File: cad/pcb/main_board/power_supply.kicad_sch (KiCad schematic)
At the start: 14 parts, among them U2 TLV75533PDRVR

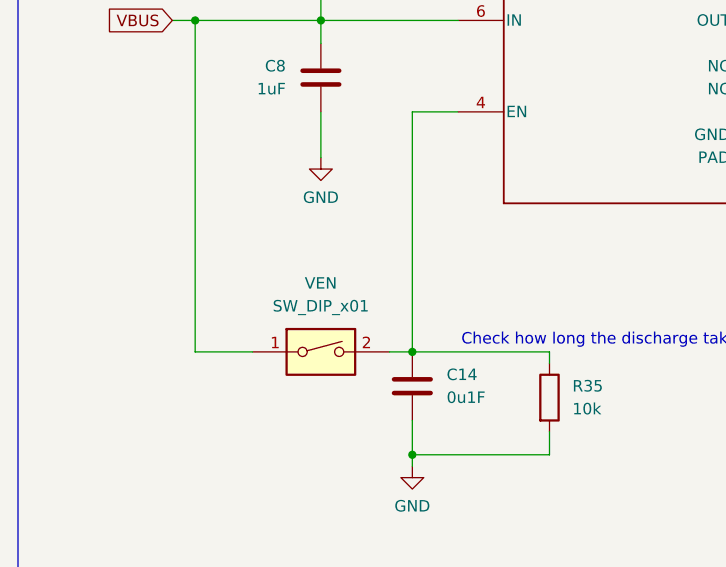
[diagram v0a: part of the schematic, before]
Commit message: Checking VBAT
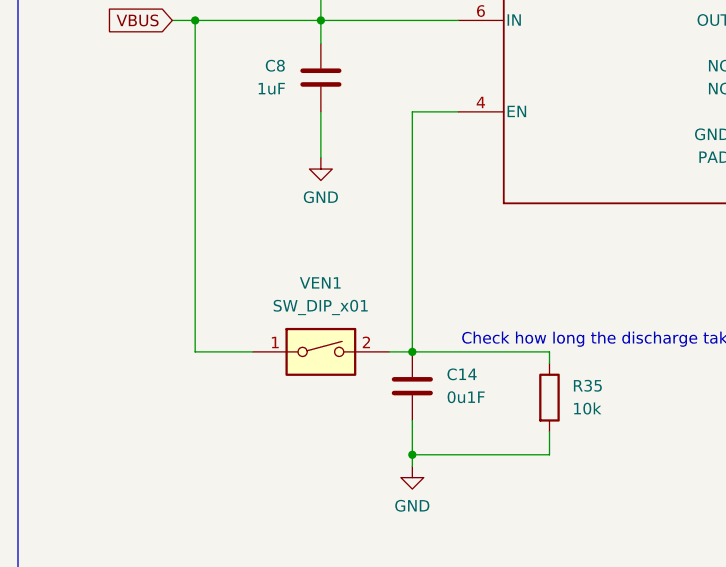
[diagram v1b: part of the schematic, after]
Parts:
- renumbered VEN to VEN1
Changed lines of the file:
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@@
 		(dnp no)
 		(fields_autoplaced yes)
-		(property "Reference" "VEN"
+		(property "Reference" "VEN1"
 			(at 80.01 151.13 0)
 			(effects
@@
 			(project "main_board"
 				(path "/6c1b8035-64fa-4797-a506-5c9583cb241c/89e1b759-e3da-4961-90e8-6f92bf79e795/8c2804c0-90ed-471e-8073-15cf7e3965b7"
-					(reference "VEN")
+					(reference "VEN1")
 					(unit 1)
 				)

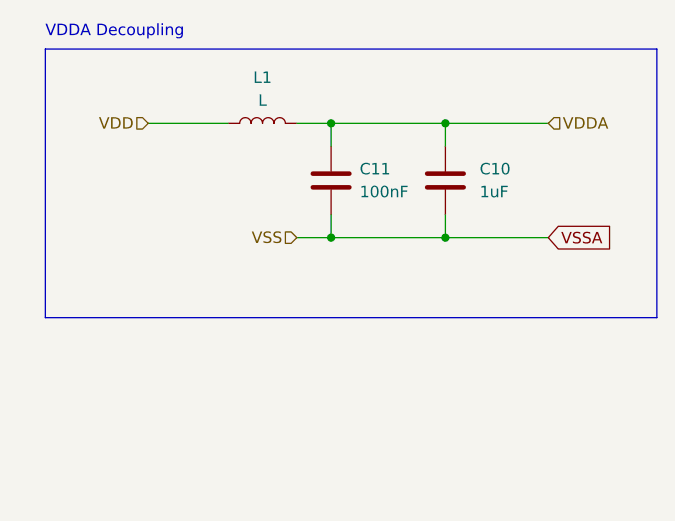
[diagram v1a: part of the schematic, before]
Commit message: DRC mostly checks out now
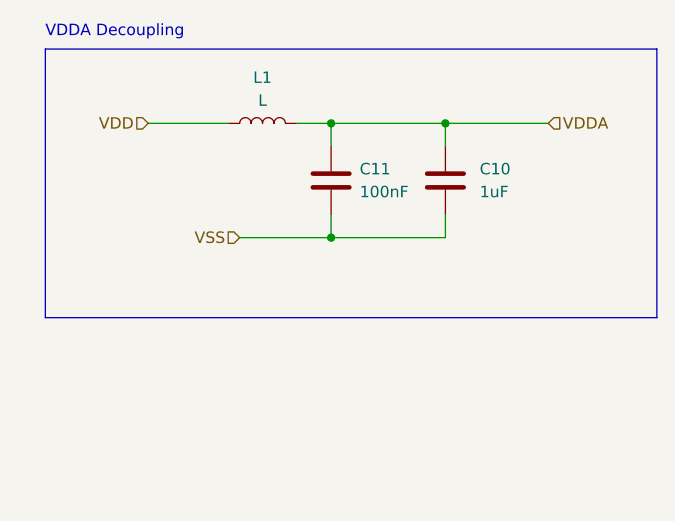
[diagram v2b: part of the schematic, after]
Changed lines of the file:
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@@
-		(color 0 0 0 0)
-	)
-	(junction
-		(at 203.2 72.39)
-		(diameter 0)
 		(color 0 0 0 0)
 	)
@@
 	(wire
 		(pts
-			(xy 214.63 72.39) (xy 203.2 72.39)
-		)
-		(stroke
-			(width 0)
-			(type default)
-		)
-	)
-	(wire
-		(pts
 			(xy 190.5 62.23) (xy 190.5 59.69)
 		)
@@
 	(wire
 		(pts
+			(xy 180.34 72.39) (xy 190.5 72.39)
+		)
+		(stroke
+			(width 0)
+			(type default)
+		)
+	)
+	(wire
+		(pts
 			(xy 102.87 72.39) (xy 102.87 69.85)
 		)
@@
 		(pts
 			(xy 170.18 59.69) (xy 179.07 59.69)
-		)
-		(stroke
-			(width 0)
-			(type default)
-		)
-	)
-	(wire
-		(pts
-			(xy 186.69 72.39) (xy 190.5 72.39)
 		)
 		(stroke
@@
 			)
 			(justify left bottom)
-		)
-	)
-	(global_label "VSSA"
-		(shape input)
-		(at 214.63 72.39 0)
-		(fields_autoplaced yes)
-		(effects
-			(font
-				(size 1.27 1.27)
-			)
-			(justify left)
-		)
-		(property "Intersheetrefs" "${INTERSHEET_REFS}"
-			(at 222.2114 72.39 0)
-			(effects
-				(font
-					(size 1.27 1.27)
-				)
-				(justify left)
-				(hide yes)
-			)
 		)
 	)
@@
 	(hierarchical_label "VSS"
 		(shape input)
-		(at 186.69 72.39 180)
+		(at 180.34 72.39 180)
 		(fields_autoplaced yes)
 		(effects

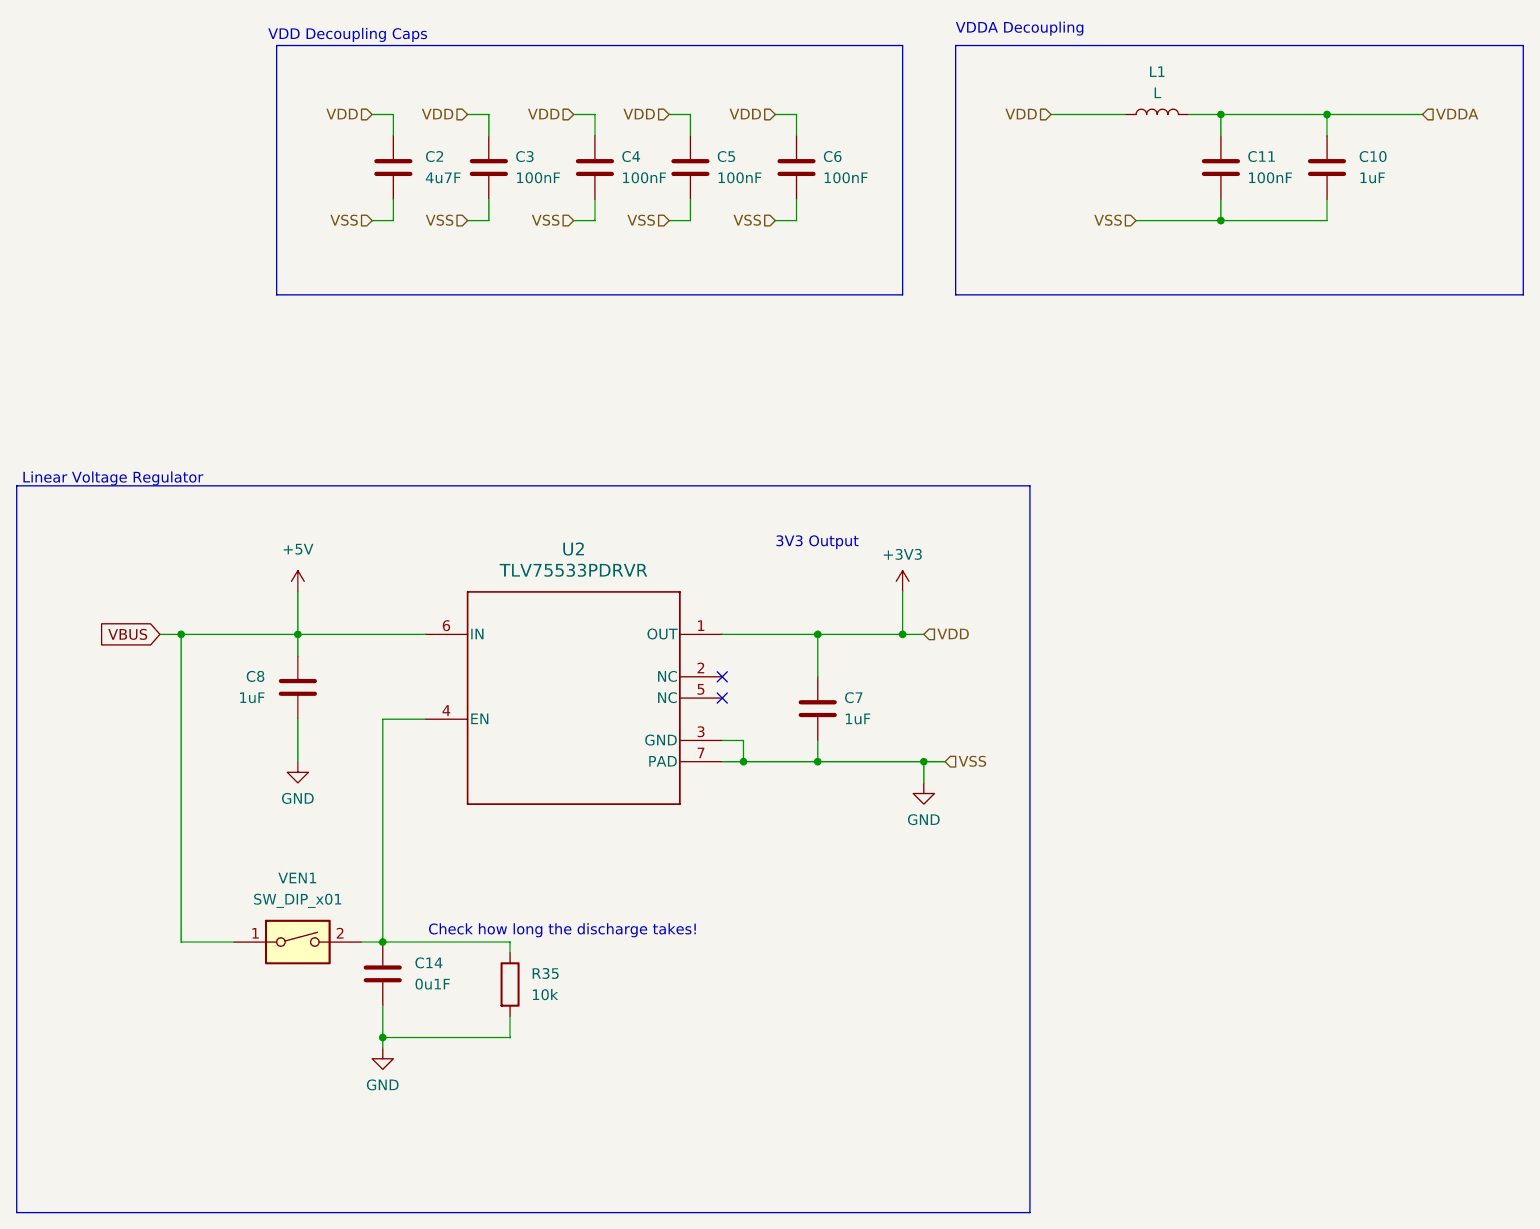
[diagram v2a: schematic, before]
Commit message: SWD connector start
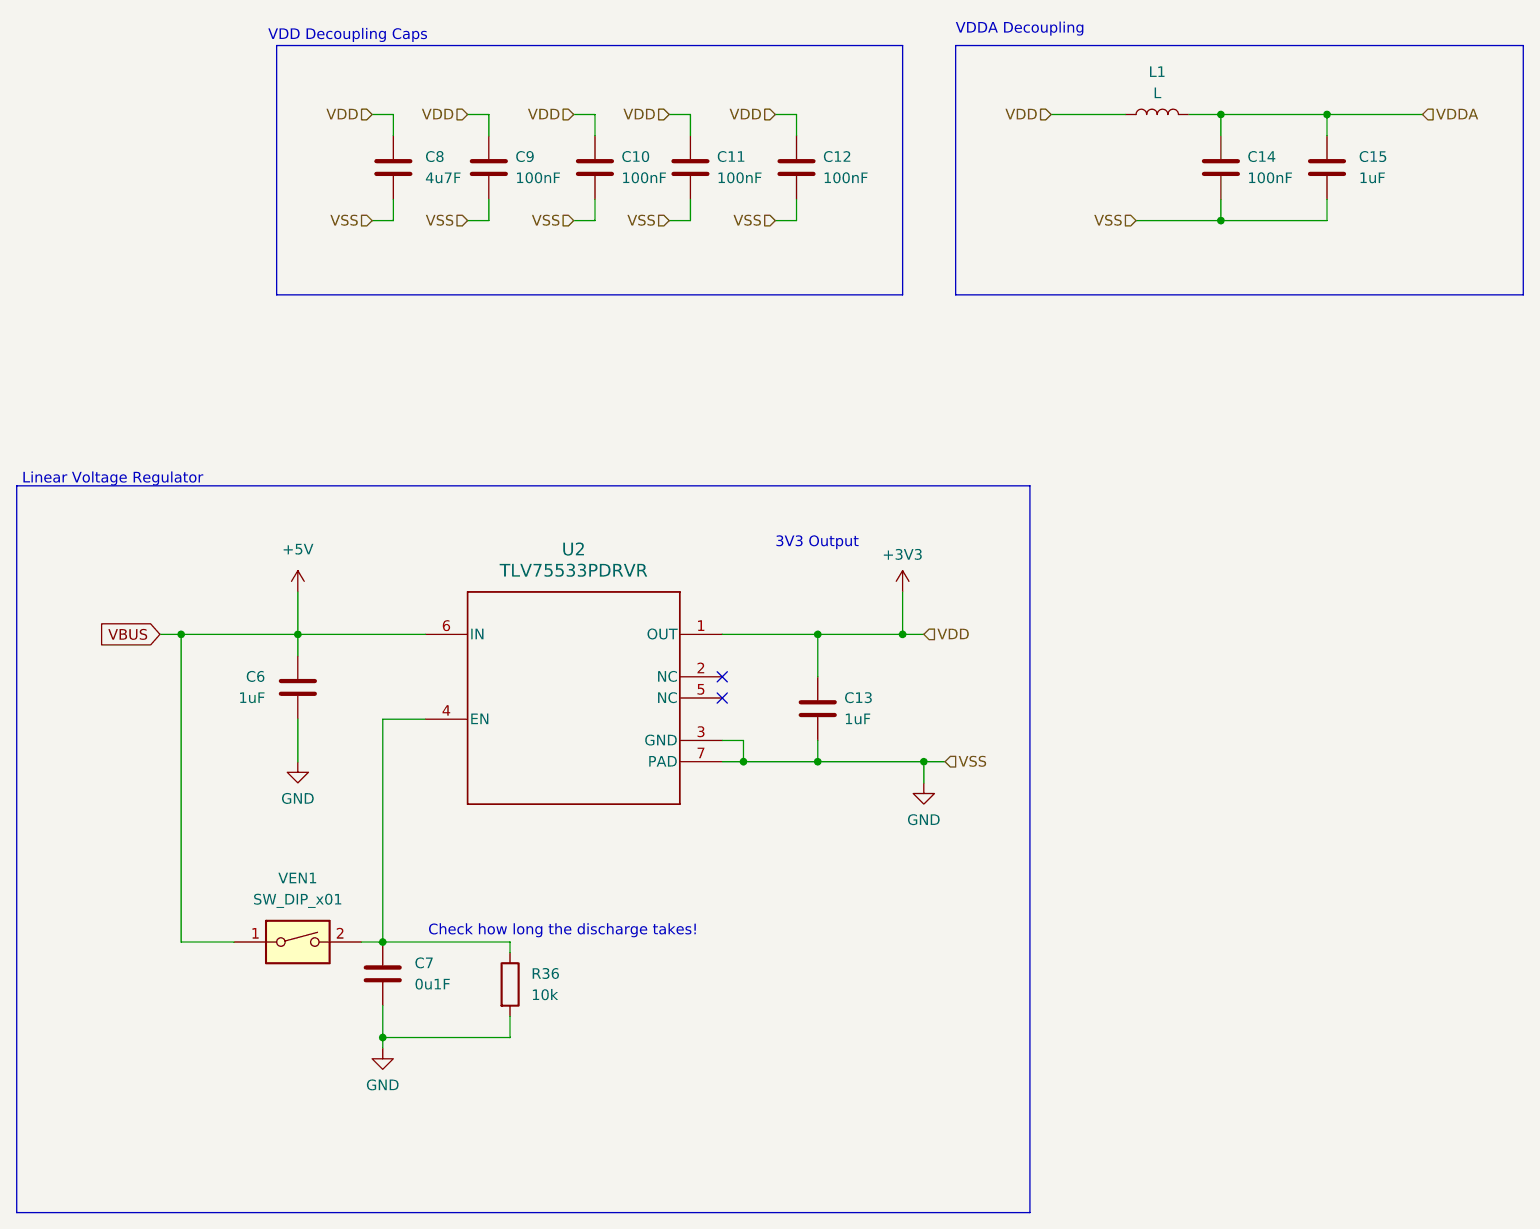
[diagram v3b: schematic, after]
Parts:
- renumbered C4 to C10, C5 to C11, C6 to C12, C7 to C13, C11 to C14, C10 to C15, C8 to C6, C14 to C7, C2 to C8, C3 to C9, R35 to R36
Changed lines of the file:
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@@
 		(dnp no)
 		(fields_autoplaced yes)
-		(property "Reference" "C5"
+		(property "Reference" "C11"
 			(at 130.175 64.77 0)
 			(effects
@@
 		(instances
 			(project "main_board"
-				(path "/6c1b8035-64fa-4797-a506-5c9583cb241c/89e1b759-e3da-4961-90e8-6f92bf79e795/8c2804c0-90ed-471e-8073-15cf7e3965b7"
-					(reference "C5")
+				(path "/6c1b8035-64fa-4797-a506-5c9583cb241c/1d8b45ae-8999-43d8-a395-f81fe3ddc1b9"
+					(reference "C11")
 					(unit 1)
 				)
@@
 		(dnp no)
 		(fields_autoplaced yes)
-		(property "Reference" "C4"
+		(property "Reference" "C10"
 			(at 118.745 64.77 0)
 			(effects
@@
 		(instances
 			(project "main_board"
-				(path "/6c1b8035-64fa-4797-a506-5c9583cb241c/89e1b759-e3da-4961-90e8-6f92bf79e795/8c2804c0-90ed-471e-8073-15cf7e3965b7"
-					(reference "C4")
+				(path "/6c1b8035-64fa-4797-a506-5c9583cb241c/1d8b45ae-8999-43d8-a395-f81fe3ddc1b9"
+					(reference "C10")
 					(unit 1)
 				)
@@
 		(on_board yes)
 		(dnp no)
-		(property "Reference" "C8"
+		(property "Reference" "C6"
 			(at 76.1166 127 0)
 			(effects
@@
 		(instances
 			(project "main_board"
-				(path "/6c1b8035-64fa-4797-a506-5c9583cb241c/89e1b759-e3da-4961-90e8-6f92bf79e795/8c2804c0-90ed-471e-8073-15cf7e3965b7"
-					(reference "C8")
+				(path "/6c1b8035-64fa-4797-a506-5c9583cb241c/1d8b45ae-8999-43d8-a395-f81fe3ddc1b9"
+					(reference "C6")
 					(unit 1)
 				)
@@
 		(dnp no)
 		(fields_autoplaced yes)
-		(property "Reference" "C11"
+		(property "Reference" "C14"
 			(at 193.675 64.77 0)
 			(effects
@@
 		(instances
 			(project "main_board"
-				(path "/6c1b8035-64fa-4797-a506-5c9583cb241c/89e1b759-e3da-4961-90e8-6f92bf79e795/8c2804c0-90ed-471e-8073-15cf7e3965b7"
-					(reference "C11")
+				(path "/6c1b8035-64fa-4797-a506-5c9583cb241c/1d8b45ae-8999-43d8-a395-f81fe3ddc1b9"
+					(reference "C14")
 					(unit 1)
 				)
@@
 		(dnp no)
 		(fields_autoplaced yes)
-		(property "Reference" "R35"
+		(property "Reference" "R36"
 			(at 107.95 162.5599 0)
 			(effects
@@
 		)
 		(instances
-			(project ""
-				(path "/6c1b8035-64fa-4797-a506-5c9583cb241c/89e1b759-e3da-4961-90e8-6f92bf79e795/8c2804c0-90ed-471e-8073-15cf7e3965b7"
-					(reference "R35")
+			(project "main_board"
+				(path "/6c1b8035-64fa-4797-a506-5c9583cb241c/1d8b45ae-8999-43d8-a395-f81fe3ddc1b9"
+					(reference "R36")
 					(unit 1)
 				)
@@
 		)
 		(instances
-			(project ""
-				(path "/6c1b8035-64fa-4797-a506-5c9583cb241c/89e1b759-e3da-4961-90e8-6f92bf79e795/8c2804c0-90ed-471e-8073-15cf7e3965b7"
+			(project "main_board"
+				(path "/6c1b8035-64fa-4797-a506-5c9583cb241c/1d8b45ae-8999-43d8-a395-f81fe3ddc1b9"
 					(reference "U2")
 					(unit 1)
@@
 		(dnp no)
 		(fields_autoplaced yes)
-		(property "Reference" "#PWR05"
+		(property "Reference" "#PWR03"
 			(at 90.17 177.8 0)
 			(effects
@@
 		(instances
 			(project "main_board"
-				(path "/6c1b8035-64fa-4797-a506-5c9583cb241c/89e1b759-e3da-4961-90e8-6f92bf79e795/8c2804c0-90ed-471e-8073-15cf7e3965b7"
-					(reference "#PWR05")
+				(path "/6c1b8035-64fa-4797-a506-5c9583cb241c/1d8b45ae-8999-43d8-a395-f81fe3ddc1b9"
+					(reference "#PWR03")
 					(unit 1)
 				)
@@
 		(dnp no)
 		(fields_autoplaced yes)
-		(property "Reference" "C6"
+		(property "Reference" "C12"
 			(at 142.875 64.77 0)
 			(effects
@@
 		(instances
 			(project "main_board"
-				(path "/6c1b8035-64fa-4797-a506-5c9583cb241c/89e1b759-e3da-4961-90e8-6f92bf79e795/8c2804c0-90ed-471e-8073-15cf7e3965b7"
-					(reference "C6")
+				(path "/6c1b8035-64fa-4797-a506-5c9583cb241c/1d8b45ae-8999-43d8-a395-f81fe3ddc1b9"
+					(reference "C12")
 					(unit 1)
 				)
@@
 		(instances
 			(project "main_board"
-				(path "/6c1b8035-64fa-4797-a506-5c9583cb241c/89e1b759-e3da-4961-90e8-6f92bf79e795/8c2804c0-90ed-471e-8073-15cf7e3965b7"
+				(path "/6c1b8035-64fa-4797-a506-5c9583cb241c/1d8b45ae-8999-43d8-a395-f81fe3ddc1b9"
 					(reference "VEN1")
 					(unit 1)
@@
 		(dnp no)
 		(fields_autoplaced yes)
-		(property "Reference" "#PWR03"
+		(property "Reference" "#PWR01"
 			(at 80.01 120.65 0)
 			(effects
@@
 		(instances
 			(project "main_board"
-				(path "/6c1b8035-64fa-4797-a506-5c9583cb241c/89e1b759-e3da-4961-90e8-6f92bf79e795/8c2804c0-90ed-471e-8073-15cf7e3965b7"
-					(reference "#PWR03")
+				(path "/6c1b8035-64fa-4797-a506-5c9583cb241c/1d8b45ae-8999-43d8-a395-f81fe3ddc1b9"
+					(reference "#PWR01")
 					(unit 1)
 				)
@@
 		(dnp no)
 		(fields_autoplaced yes)
-		(property "Reference" "#PWR04"
+		(property "Reference" "#PWR02"
 			(at 80.01 143.51 0)
 			(effects
@@
 		(instances
 			(project "main_board"
-				(path "/6c1b8035-64fa-4797-a506-5c9583cb241c/89e1b759-e3da-4961-90e8-6f92bf79e795/8c2804c0-90ed-471e-8073-15cf7e3965b7"
-					(reference "#PWR04")
+				(path "/6c1b8035-64fa-4797-a506-5c9583cb241c/1d8b45ae-8999-43d8-a395-f81fe3ddc1b9"
+					(reference "#PWR02")
 					(unit 1)
 				)
@@
 		(dnp no)
 		(fields_autoplaced yes)
-		(property "Reference" "C10"
+		(property "Reference" "C15"
 			(at 207.01 64.77 0)
 			(effects
@@
 		(instances
 			(project "main_board"
-				(path "/6c1b8035-64fa-4797-a506-5c9583cb241c/89e1b759-e3da-4961-90e8-6f92bf79e795/8c2804c0-90ed-471e-8073-15cf7e3965b7"
-					(reference "C10")
+				(path "/6c1b8035-64fa-4797-a506-5c9583cb241c/1d8b45ae-8999-43d8-a395-f81fe3ddc1b9"
+					(reference "C15")
 					(unit 1)
 				)
@@
 		(dnp no)
 		(fields_autoplaced yes)
-		(property "Reference" "#PWR01"
+		(property "Reference" "#PWR05"
 			(at 154.94 146.05 0)
 			(effects
@@
 		(instances
 			(project "main_board"
-				(path "/6c1b8035-64fa-4797-a506-5c9583cb241c/89e1b759-e3da-4961-90e8-6f92bf79e795/8c2804c0-90ed-471e-8073-15cf7e3965b7"
-					(reference "#PWR01")
+				(path "/6c1b8035-64fa-4797-a506-5c9583cb241c/1d8b45ae-8999-43d8-a395-f81fe3ddc1b9"
+					(reference "#PWR05")
 					(unit 1)
 				)
@@
 		(dnp no)
 		(fields_autoplaced yes)
-		(property "Reference" "C3"
+		(property "Reference" "C9"
 			(at 106.045 64.77 0)
 			(effects
@@
 		(instances
 			(project "main_board"
-				(path "/6c1b8035-64fa-4797-a506-5c9583cb241c/89e1b759-e3da-4961-90e8-6f92bf79e795/8c2804c0-90ed-471e-8073-15cf7e3965b7"
-					(reference "C3")
+				(path "/6c1b8035-64fa-4797-a506-5c9583cb241c/1d8b45ae-8999-43d8-a395-f81fe3ddc1b9"
+					(reference "C9")
 					(unit 1)
 				)
@@
 		(dnp no)
 		(fields_autoplaced yes)
-		(property "Reference" "#PWR02"
+		(property "Reference" "#PWR04"
 			(at 152.4 120.65 0)
 			(effects
@@
 		(instances
 			(project "main_board"
-				(path "/6c1b8035-64fa-4797-a506-5c9583cb241c/89e1b759-e3da-4961-90e8-6f92bf79e795/8c2804c0-90ed-471e-8073-15cf7e3965b7"
-					(reference "#PWR02")
+				(path "/6c1b8035-64fa-4797-a506-5c9583cb241c/1d8b45ae-8999-43d8-a395-f81fe3ddc1b9"
+					(reference "#PWR04")
 					(unit 1)
 				)
@@
 		(dnp no)
 		(fields_autoplaced yes)
-		(property "Reference" "C7"
+		(property "Reference" "C13"
 			(at 145.415 129.54 0)
 			(effects
@@
 		(instances
 			(project "main_board"
-				(path "/6c1b8035-64fa-4797-a506-5c9583cb241c/89e1b759-e3da-4961-90e8-6f92bf79e795/8c2804c0-90ed-471e-8073-15cf7e3965b7"
-					(reference "C7")
+				(path "/6c1b8035-64fa-4797-a506-5c9583cb241c/1d8b45ae-8999-43d8-a395-f81fe3ddc1b9"
+					(reference "C13")
 					(unit 1)
 				)
@@
 		(instances
 			(project "main_board"
-				(path "/6c1b8035-64fa-4797-a506-5c9583cb241c/89e1b759-e3da-4961-90e8-6f92bf79e795/8c2804c0-90ed-471e-8073-15cf7e3965b7"
+				(path "/6c1b8035-64fa-4797-a506-5c9583cb241c/1d8b45ae-8999-43d8-a395-f81fe3ddc1b9"
 					(reference "L1")
 					(unit 1)
@@
 		(dnp no)
 		(fields_autoplaced yes)
-		(property "Reference" "C14"
+		(property "Reference" "C7"
 			(at 93.98 161.29 0)
 			(effects
@@
 		(instances
 			(project "main_board"
-				(path "/6c1b8035-64fa-4797-a506-5c9583cb241c/89e1b759-e3da-4961-90e8-6f92bf79e795/8c2804c0-90ed-471e-8073-15cf7e3965b7"
-					(reference "C14")
+				(path "/6c1b8035-64fa-4797-a506-5c9583cb241c/1d8b45ae-8999-43d8-a395-f81fe3ddc1b9"
+					(reference "C7")
 					(unit 1)
 				)
@@
 		(dnp no)
 		(fields_autoplaced yes)
-		(property "Reference" "C2"
+		(property "Reference" "C8"
 			(at 95.25 64.77 0)
 			(effects
@@
 		(instances
 			(project "main_board"
-				(path "/6c1b8035-64fa-4797-a506-5c9583cb241c/89e1b759-e3da-4961-90e8-6f92bf79e795/8c2804c0-90ed-471e-8073-15cf7e3965b7"
-					(reference "C2")
-					(unit 1)
-				)
+				(path "/6c1b8035-64fa-4797-a506-5c9583cb241c/1d8b45ae-8999-43d8-a395-f81fe3ddc1b9"
+					(reference "C8")
+					(unit 1)
+				)
